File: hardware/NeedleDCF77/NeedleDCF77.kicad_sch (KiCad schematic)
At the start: 44 parts, among them J1 USB_C_Receptacle_USB2.0, U2 STM32L051C8Tx

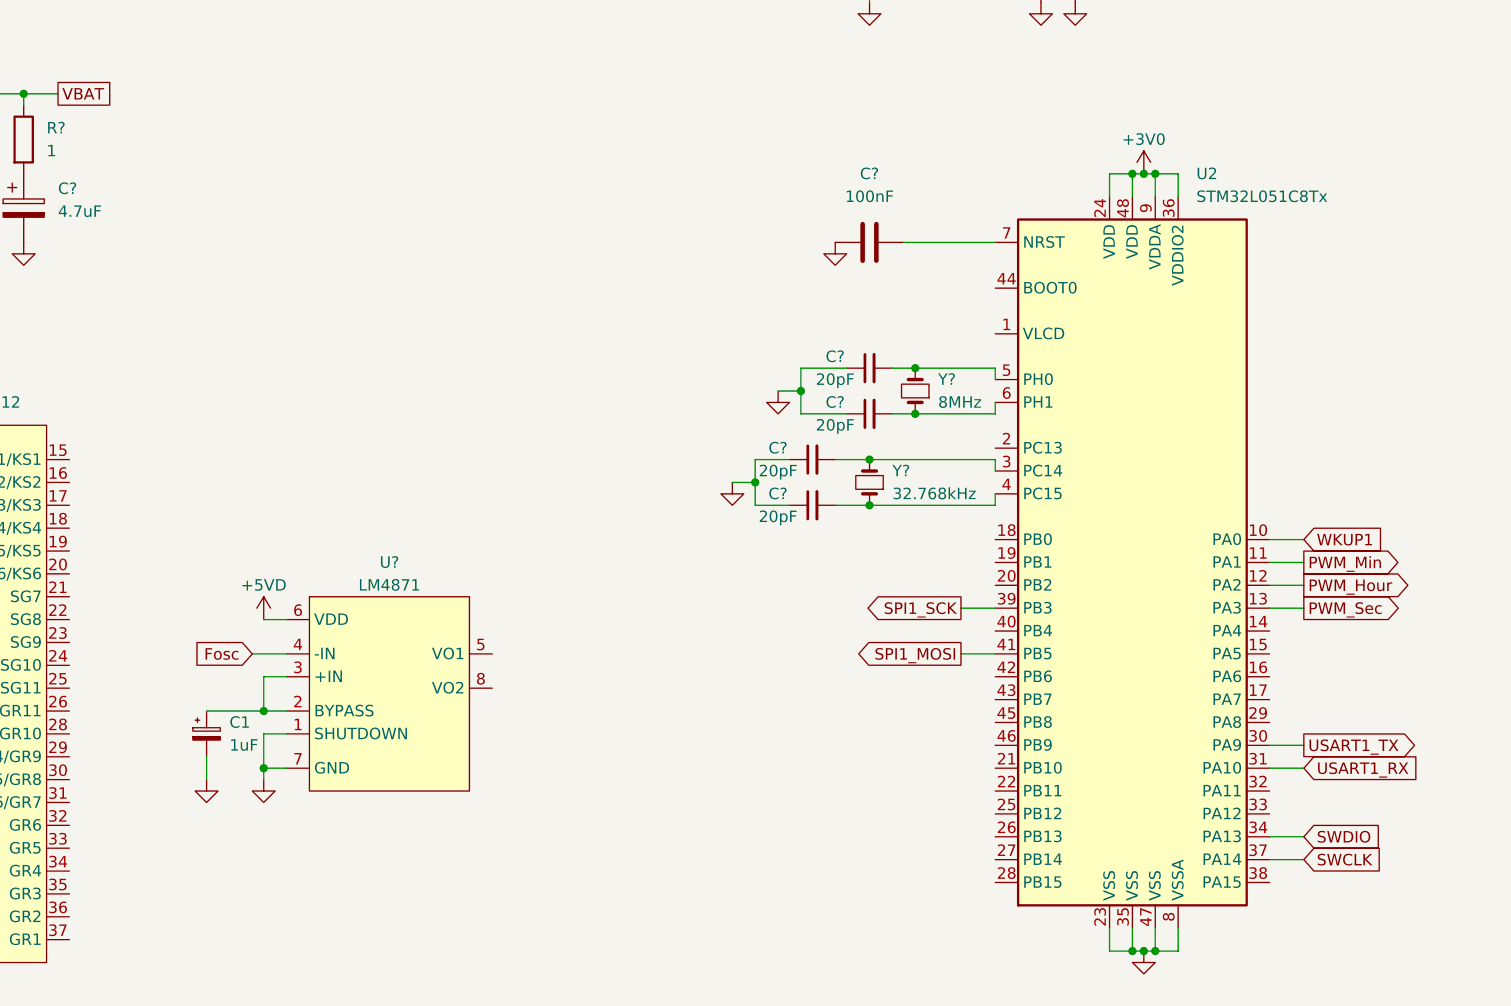
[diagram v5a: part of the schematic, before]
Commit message: Create -24V power supply
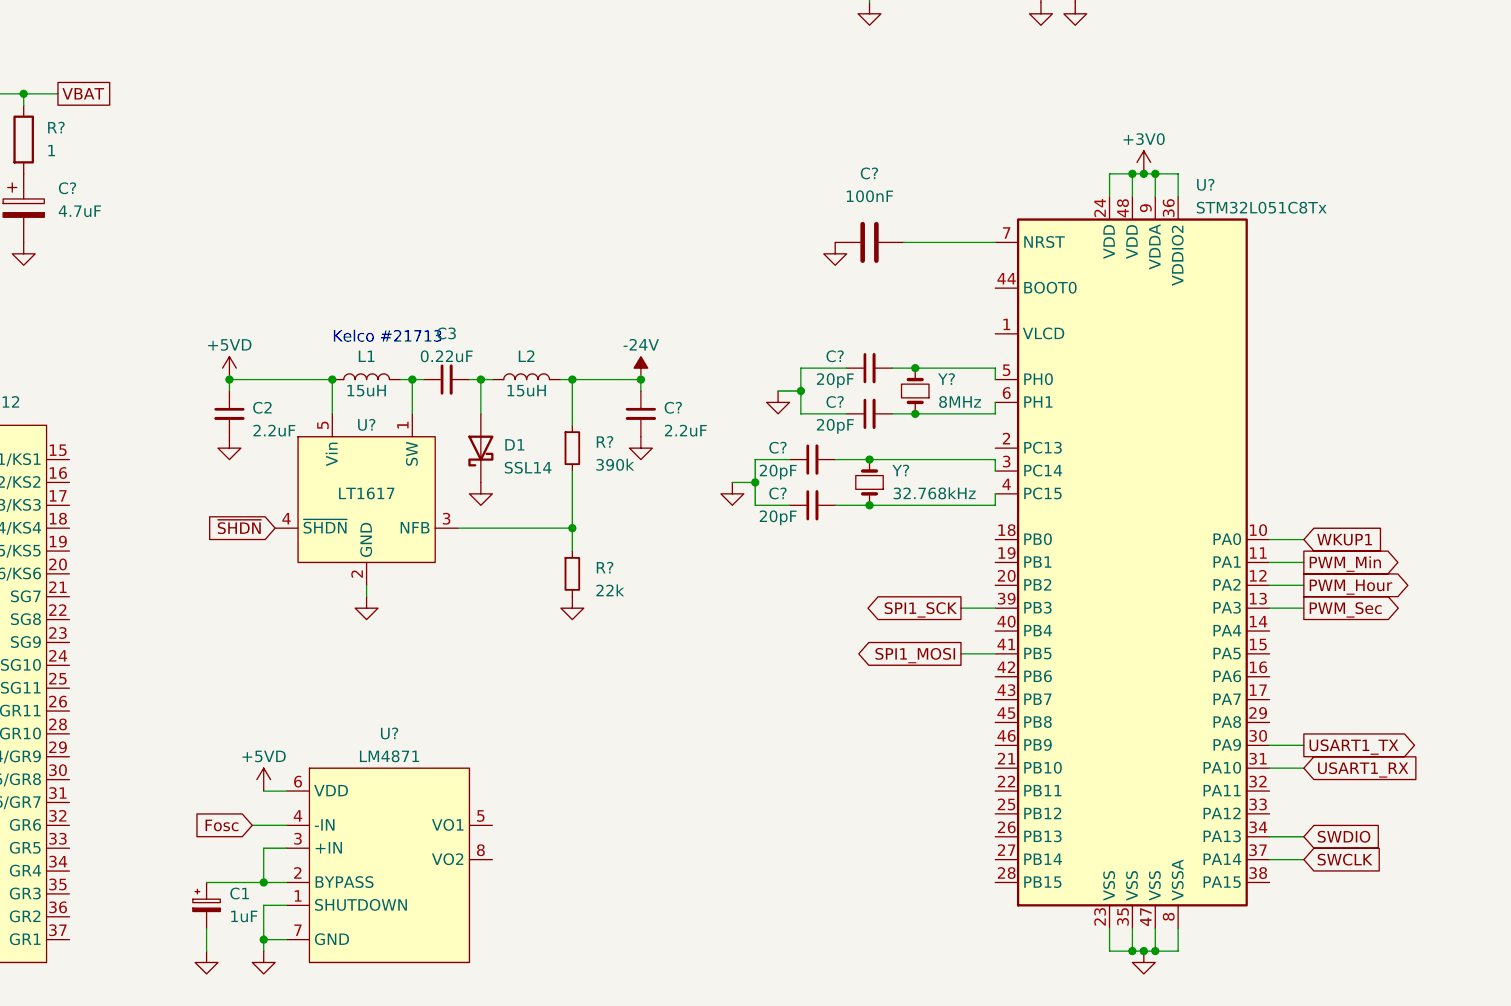
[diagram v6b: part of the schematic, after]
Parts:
- added C2, C?: 2.2uF, symbol Device:C_Small
- added C3: 0.22uF, symbol Device:C_Small
- added D1: SSL14, symbol Device:D_Schottky
- added L1, L2: 15uH, symbol Device:L
- added R?: 22k, symbol Device:R_Small
- added R?: 390k, symbol Device:R_Small
- added U?: LT1617, Package_TO_SOT_SMD:SOT-23-5_HandSoldering, symbol Inverting_switching_regulator:LT1617
- renumbered U2 to U?
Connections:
- net +5VD: now also C2.1, L1.1, U?.5 (Vin)
- net GND: now also C2.2, C?.2, D1.1 (K), R?.2, U?.2 (GND)
- new net: R?.1, R?.2, U?.3 (NFB)
- new net: C3.2, D1.2 (A), L2.1
- new net: C3.1, L1.2, U?.1 (SW)
- new net -24V: C?.1, L2.2, R?.1
- new net ~{SHDN}: U?.4 (~{SHDN})
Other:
- note added: "Kelco #21713"
- moved on the sheet: C1, U?

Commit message: Implement VFD circuit
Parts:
- added C?: C_Small, symbol Device:C_Small
- added C? (x2): 4.7uF, symbol Device:C_Polarized_Small
- added D?: 6.2V, symbol Device:D_Zener_Small
- added R?: 10k, symbol Device:R_Small
- added R? (x2): 470, symbol Device:R_Small
- added R? (x2): 3R9, symbol Device:R_Small
- added R?: 51k, symbol Device:R_Small
- added VFD?: FG95A, VFD:FG95A, symbol VFD:FG95A
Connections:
- net +3V0: now also R?.1
- net +5VD: now also U?.14 (VDD), U?.38 (VDD), R?.1
- net -24V: now also U?.27 (VEE), C?.1, D?.2 (A)
- net GND: now also U?.43 (GND), U?.7 (GND), C?.2
- net SPI1_MOSI: now also U?.6 (DIN)
- net SPI1_SCK: now also U?.8 (CLK)
- net SG1: now reaches U?.15 (SG1/KS1)
- net SG1: now also VFD?.18 (Sa)
- net SG2: now reaches U?.16 (SG2/KS2)
- net SG2: now also VFD?.17 (Sb)
- net SG3: now reaches U?.17 (SG3/KS3)
- net SG3: now also VFD?.16 (Sc)
- net SG4: now reaches U?.18 (SG4/KS4)
- net SG4: now also VFD?.15 (Sd)
- net SG5: now reaches U?.19 (SG5/KS5)
- net SG5: now also VFD?.4 (Se)
- net SG6: now reaches U?.20 (SG6/KS6)
- net SG6: now also VFD?.2 (Sf)
- net SG7: now reaches U?.21 (SG7)
- net SG7: now also VFD?.3 (Sg)
- net SG8: now reaches U?.22 (SG8)
- net SG8: now also VFD?.5 (Sdot)
- net GR9: now reaches U?.29 (SG14/GR9)
- net GR9: now also VFD?.14 (G9)
- net GR8: now reaches U?.30 (SG15/GR8)
- net GR8: now also VFD?.13 (G8)
- net GR7: now reaches U?.31 (SG16/GR7)
- net GR7: now also VFD?.12 (G7)
- net GR6: now reaches U?.32 (GR6)
- net GR6: now also VFD?.11 (G6)
- net GR5: now reaches U?.33 (GR5)
- net GR5: now also VFD?.10 (G5)
- net GR4: now reaches U?.34 (GR4)
- net GR4: now also VFD?.9 (G4)
- net GR3: now reaches U?.35 (GR3)
- net GR3: now also VFD?.8 (G3)
- net GR2: now reaches U?.36 (GR2)
- net GR2: now also VFD?.7 (G2)
- net GR1: now reaches U?.37 (GR1)
- net GR1: now also VFD?.6 (G1)
- net at U?.44 (OSC): now also R?.2
- net SPI1_MISO: now reaches U?.5 (DOUT)
- net SPI1_MISO: now also U?.40 (PB4), R?.2
- net SPI1_NSS: now reaches U?.9 (STB)
- net SPI1_NSS: now also U?.14 (PA4)
- net FOSC: now reaches U?.15 (PA5)
- net at U?.5 (VO1): now also C?.1
- net at U?.8 (VO2): now also C?.1
- new net: C?.2, R?.1, R?.1 (x2)
- new net: D?.1 (K), R?.2, R?.2
- new net AC1: R?.2, VFD?.1 (F1)
- new net AC2: R?.2, VFD?.19 (F2)
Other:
- note added: "BIAS"
- moved on the sheet: C1, C2, C3, C?, D1, D?, F?, J1, J?, L1, L2, R?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

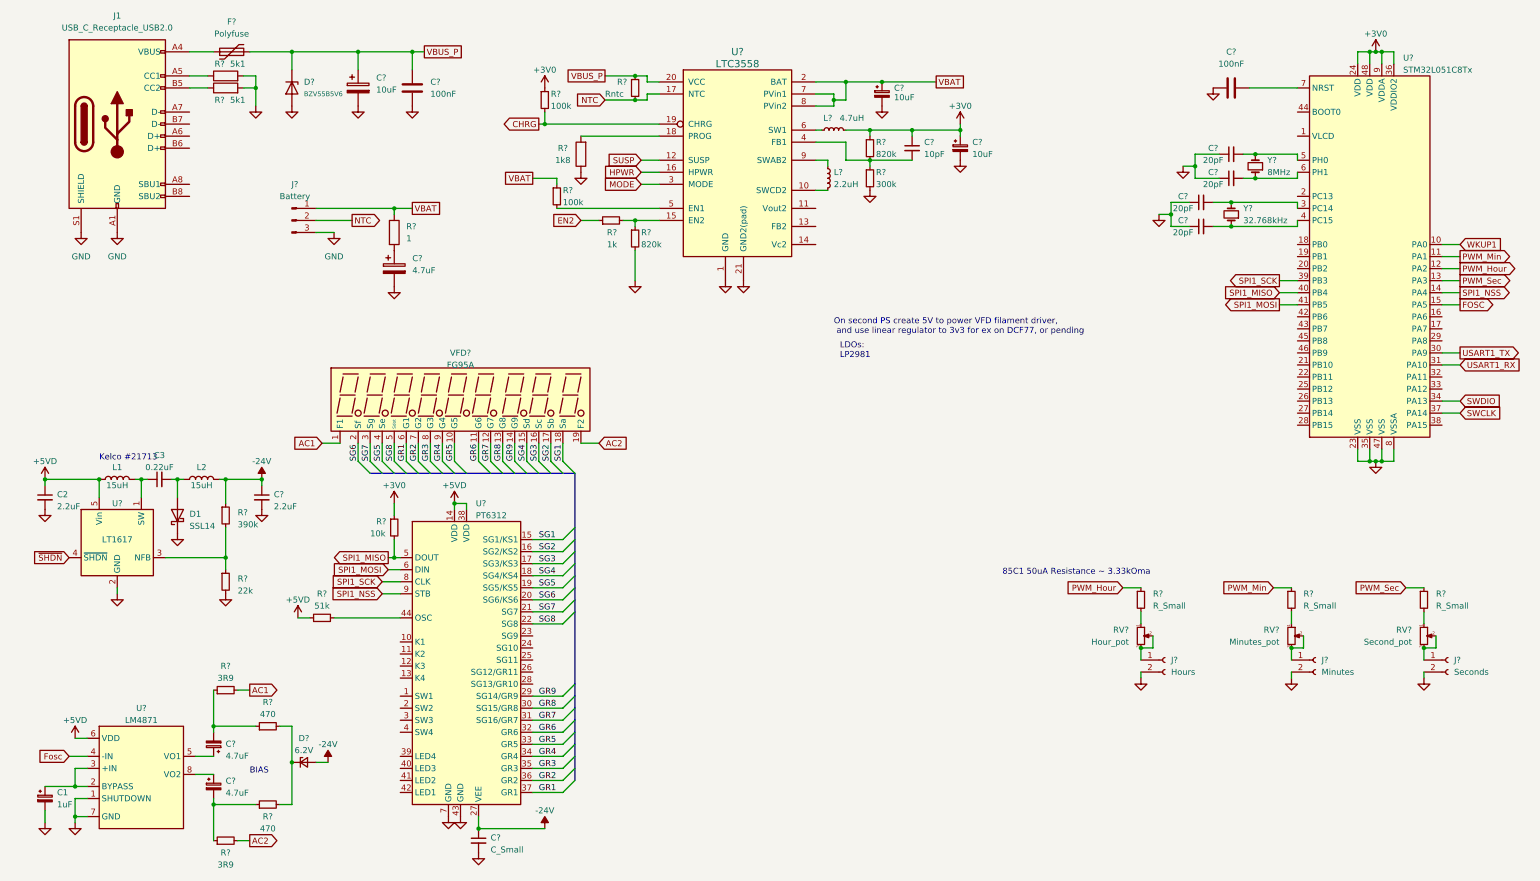
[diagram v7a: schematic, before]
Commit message: Implement 5V for VFD circuitry
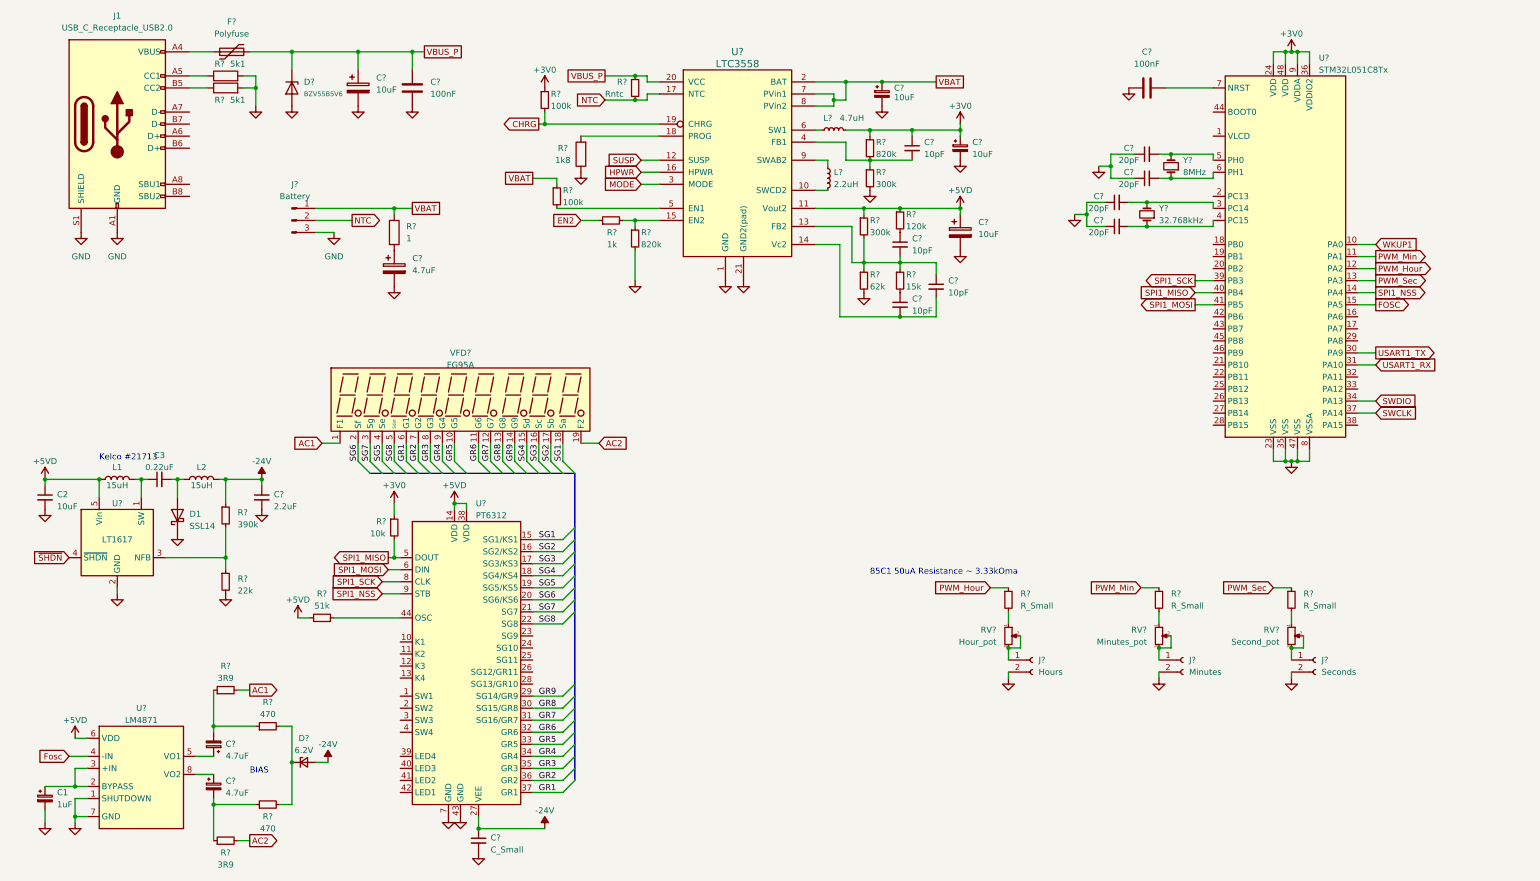
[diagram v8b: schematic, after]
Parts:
- added C? (x3): 10pF, symbol Device:C_Small
- added C?: 10uF, symbol Device:C_Polarized
- added R?: 300k, symbol Device:R_Small
- added R?: 120k, symbol Device:R_Small
- added R?: 15k, symbol Device:R_Small
- added R?: 62k, symbol Device:R_Small
- C2: value 2.2uF -> 10uF
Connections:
- net +5VD: now also U?.11 (Vout2), C?.1, R?.1, R?.1
- net GND: now also C?.2, R?.2
- net at U?.13 (FB2): now also C?.1, C?.2, R?.1, R?.1, R?.2
- net at U?.14 (Vc2): now also C?.2, C?.2
- new net: C?.1, R?.2 (x2)
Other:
- note removed: "LDOs: LP2981"
- note removed: "On second PS create 5V to power VFD filament driver, and use linear regulator to 3v3 for ex on DCF77, or pending"
- moved on the sheet: C?, J?, R?, RV?, U?, Y?
